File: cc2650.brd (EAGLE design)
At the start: 50.8 x 22.9 mm, 26 parts, among them IC1 TPS73133DBVR, IC4 CC2650MODAMOHR, SW1 SPST_TACT-KMR2, SW3 SPST_TACT-KMR2

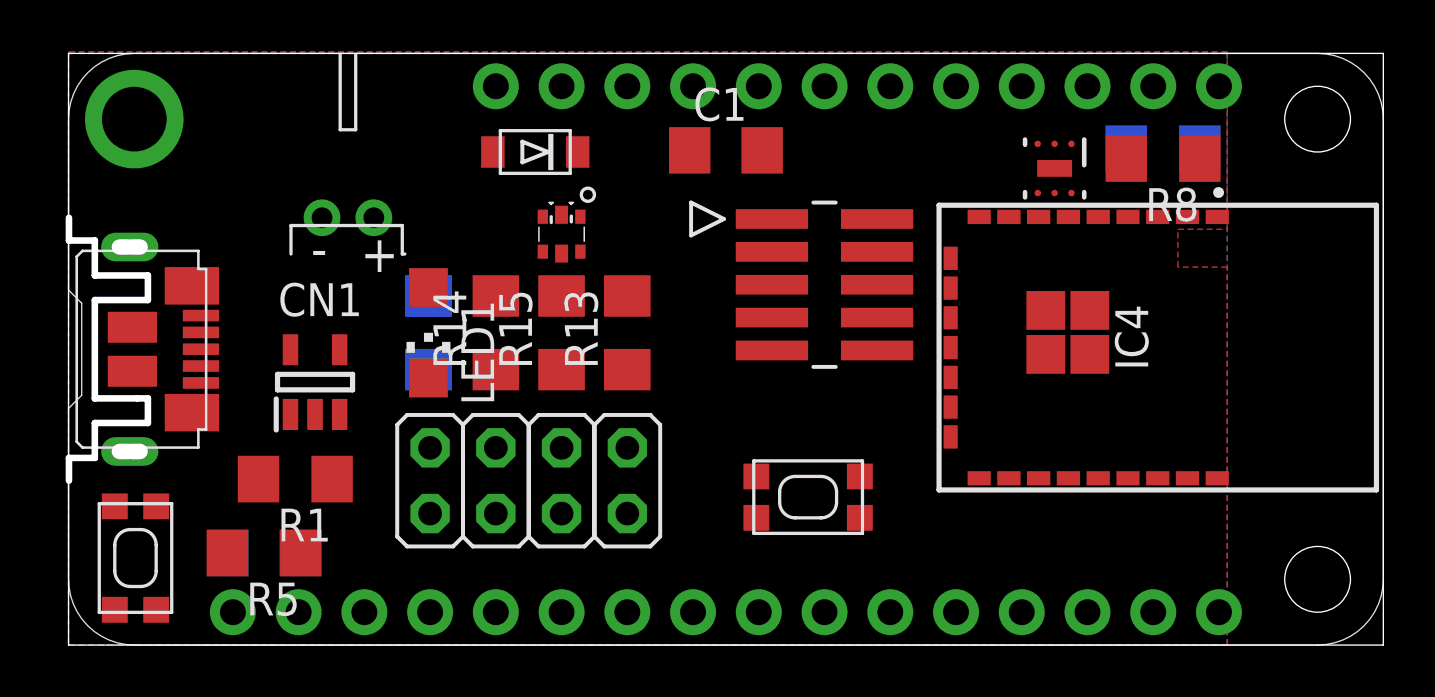
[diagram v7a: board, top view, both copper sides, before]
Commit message: removed RGB LED. Removed extra power pins from pin headers.
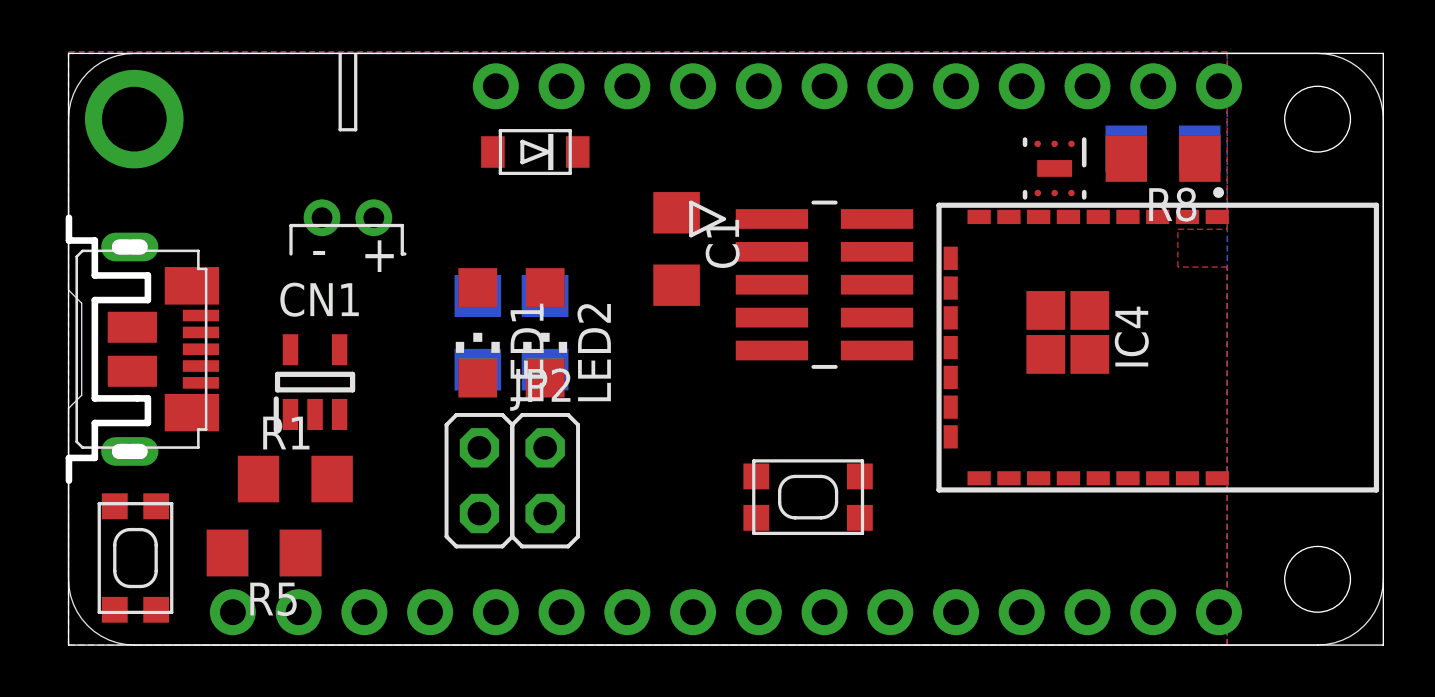
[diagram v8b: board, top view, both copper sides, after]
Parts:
- removed JP4: LED2_RED, jumper:JP1M
- removed JP5: LED2_GREEN, jumper:JP1M
- removed JP6: LED2_BLUE, jumper:JP1M
- removed LED5: EVERLIGHT_19-337, MSP-EXP432:RGB_LED
- removed R13: 24, adafruit:R1206
- removed R14: 16, adafruit:R1206
- removed R15: 110, adafruit:R1206
- added JP2: GPIO_LED, jumper:JP1M
- added LED2: RED, adafruit:CHIPLED_1206
- added R2: 470, adafruit:R1206
- JP1: value LED1 -> PWR_LED
- moved C1 4.26 mm to (23.5, 15.3), turned to 270 degrees
- moved LED1 1.91 mm to (15.8, 12.1)
- moved R3 1.91 mm to (15.8, 12.1)
- moved JP1 1.90 mm to (15.9, 6.35)
- turned R1 to 0 degrees
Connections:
- removed net N$12: JP6.2, R13.1
- removed net N$5: LED5.6, R14.2
- removed net N$6: LED5.4, R13.2
- removed net N$7: JP5.2, R14.1
- removed net P2.0_RGBLED_RED: JP4.1
- removed net P2.1_RGBLED_GREEN: JP5.1
- removed net P2.2_RGBLED_BLUE: JP6.1
- new net N$2: LED2.A, R2.2
- net GND: now also LED2.C; no longer LED5.1, LED5.2, LED5.3, MS1.23, MS1.24
- net N$3: now also JP2.2, R2.1; no longer JP4.2, R15.1
- net N$4: now also JP2.1; no longer LED5.5, R15.2
- net VCC: no longer MS1.25, MS1.3
